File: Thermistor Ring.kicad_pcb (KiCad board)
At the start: 2 copper layers, 70 x 70 mm, 20 parts, among them IC1 MAX30210ENL+, IC2 MAX30210ENL+, IC3 MAX30210ENL+, IC4 MAX30210ENL+, IC5 MAX30210ENL+, IC6 MAX30210ENL+, J1 Conn_01x04_Socket, J3 Conn_01x03_Socket, U1 TPS7A2018PDBVR

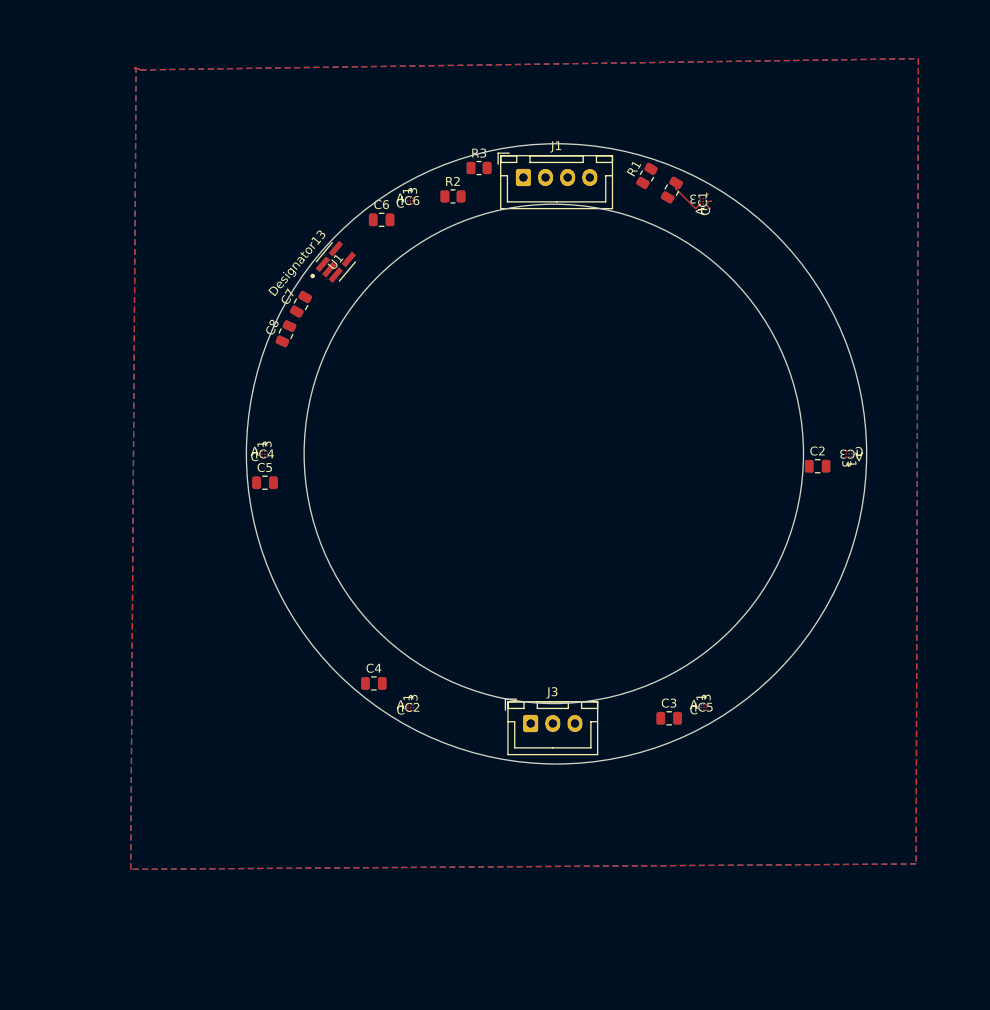
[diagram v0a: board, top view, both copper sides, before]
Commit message: saving before moving thermistors
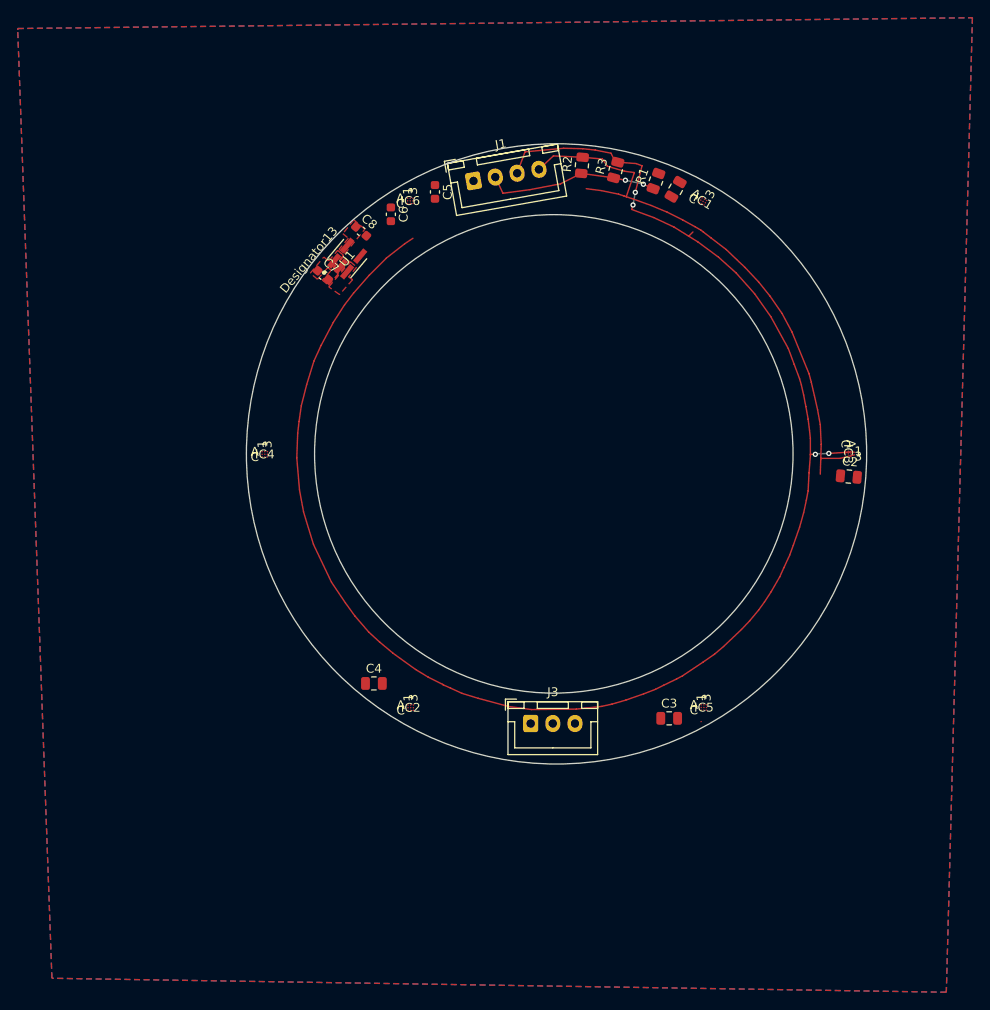
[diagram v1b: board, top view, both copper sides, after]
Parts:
- C5, C6, C7, C8: footprint Capacitor_SMD:C_0805_2012Metric -> Capacitor_SMD:C_0603_1608Metric
- moved C5 38.0 mm to (200.2, 41.6), turned to -90 degrees
- moved R3 15.4 mm to (220.6, 39.1), turned to 75 degrees
- moved R2 15.0 mm to (216.8, 38.6), turned to 85 degrees
- moved C8 14.3 mm to (191.9, 46.0), turned to -40 degrees
- moved J1 5.64 mm to (204.5, 40.3), turned to 10 degrees
- moved C7 4.13 mm to (187.6, 50.9), turned to -40 degrees
- moved C2 3.70 mm to (246.9, 73.7), turned to -5 degrees
- moved U1 1.34 mm to (190.3, 49.1)
- moved C6 1.21 mm to (195.2, 44.1), turned to -90 degrees
- moved R1 1.16 mm to (225.1, 40.3), turned to 70 degrees
- moved C1 0.43 mm to (227.4, 41.3), turned to 60 degrees
- moved IC3 0.10 mm to (246.8, 71.1), turned to -90 degrees
- turned IC1 to -30 degrees
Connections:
- net Net-(IC1-VDD) renamed /VDD
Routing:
- net /SDA: track 0.74 -> 183.6 mm, vias 0 -> 4
- net /SCL: track 0.66 -> 64.7 mm
- net /Power 3.3-5V: track 0.00 -> 19.6 mm, vias 0 -> 2
- net /VDD: track 4.57 -> 0.00 mm
- net /CVT/PDB: track 0.83 -> 0.00 mm
- added copper zone on F.Cu, net /ENABLE
- added copper zone on F.Cu, net /Power 3.3-5V
- added copper zone on F.Cu, net /VDD
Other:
- outline, holes or cut-outs redrawn

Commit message: v0.1 alpha for review
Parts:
- U1: footprint LDO_TSA7A:DBV0005A-IPC_A -> TPS7A201:DBV0005A-IPC_A
- moved R2 32.3 mm to (188.1, 53.6), turned to -35 degrees
- moved R3 32.1 mm to (190.6, 50.5), turned to -40 degrees
- moved R1 32.0 mm to (193.9, 47.3), turned to -50 degrees
- moved C6 26.2 mm to (182.8, 67.2), turned to -10 degrees
- moved C8 19.2 mm to (184.8, 63.9), turned to 160 degrees
- moved U1 12.9 mm to (185.2, 61.0), turned to -110 degrees
- moved C1 7.66 mm to (232.8, 46.7), turned to -130 degrees
- moved C7 7.40 mm to (187.2, 58.3), turned to 160 degrees
- moved J3 5.28 mm to (216.3, 102.1), turned to 180 degrees
- moved C2 2.59 mm to (244.4, 74.3)
- moved C4 2.36 mm to (195.5, 96.3), turned to 55 degrees
- moved IC5 2.27 mm to (229.1, 98.0), turned to -150 degrees
- moved IC3 2.24 mm to (244.6, 71.1), turned to 0 degrees
- moved IC1 2.11 mm to (229.1, 44.3), turned to -100 degrees
- moved C3 1.96 mm to (224.9, 100.1), turned to 115 degrees
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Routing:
- net /VDD: track 0.00 -> 244.5 mm, vias 0 -> 20
- net /CVT/PDB: track 0.00 -> 224.6 mm, vias 0 -> 13
- net /INT: track 0.00 -> 213.3 mm, vias 0 -> 8
- net GND: track 0.00 -> 195.9 mm, vias 0 -> 18
- net /SCL: track 64.7 -> 196.8 mm, vias 0 -> 13
- net /ENABLE: track 0.00 -> 61.8 mm, vias 0 -> 4
- net /Power 3.3-5V: track 19.6 -> 38.4 mm, vias 2 -> 0
- net /SDA: track 183.6 -> 202.3 mm
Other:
- outline, holes or cut-outs redrawn

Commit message: changing to smaller diameter
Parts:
- moved IC2 123.2 mm to (75.4, 87.0)
- moved IC6 123.2 mm to (75.4, 33.3)
- moved J1 123.2 mm to (82.5, 30.3)
- moved R3 123.2 mm to (68.0, 39.6)
- moved C1 123.2 mm to (110.1, 35.7)
- moved C4 123.2 mm to (72.9, 85.3)
- moved C5 123.2 mm to (78.3, 31.8)
- moved C6 123.2 mm to (60.1, 56.2)
- moved IC1 123.2 mm to (106.4, 33.3)
- moved IC5 123.2 mm to (106.4, 87.0)
- moved R1 123.2 mm to (71.2, 36.3)
- moved U1 123.2 mm to (62.5, 50.0)
- moved C2 123.2 mm to (121.7, 63.3)
- moved C3 123.2 mm to (102.2, 89.1)
- moved C7 123.2 mm to (64.6, 47.4)
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
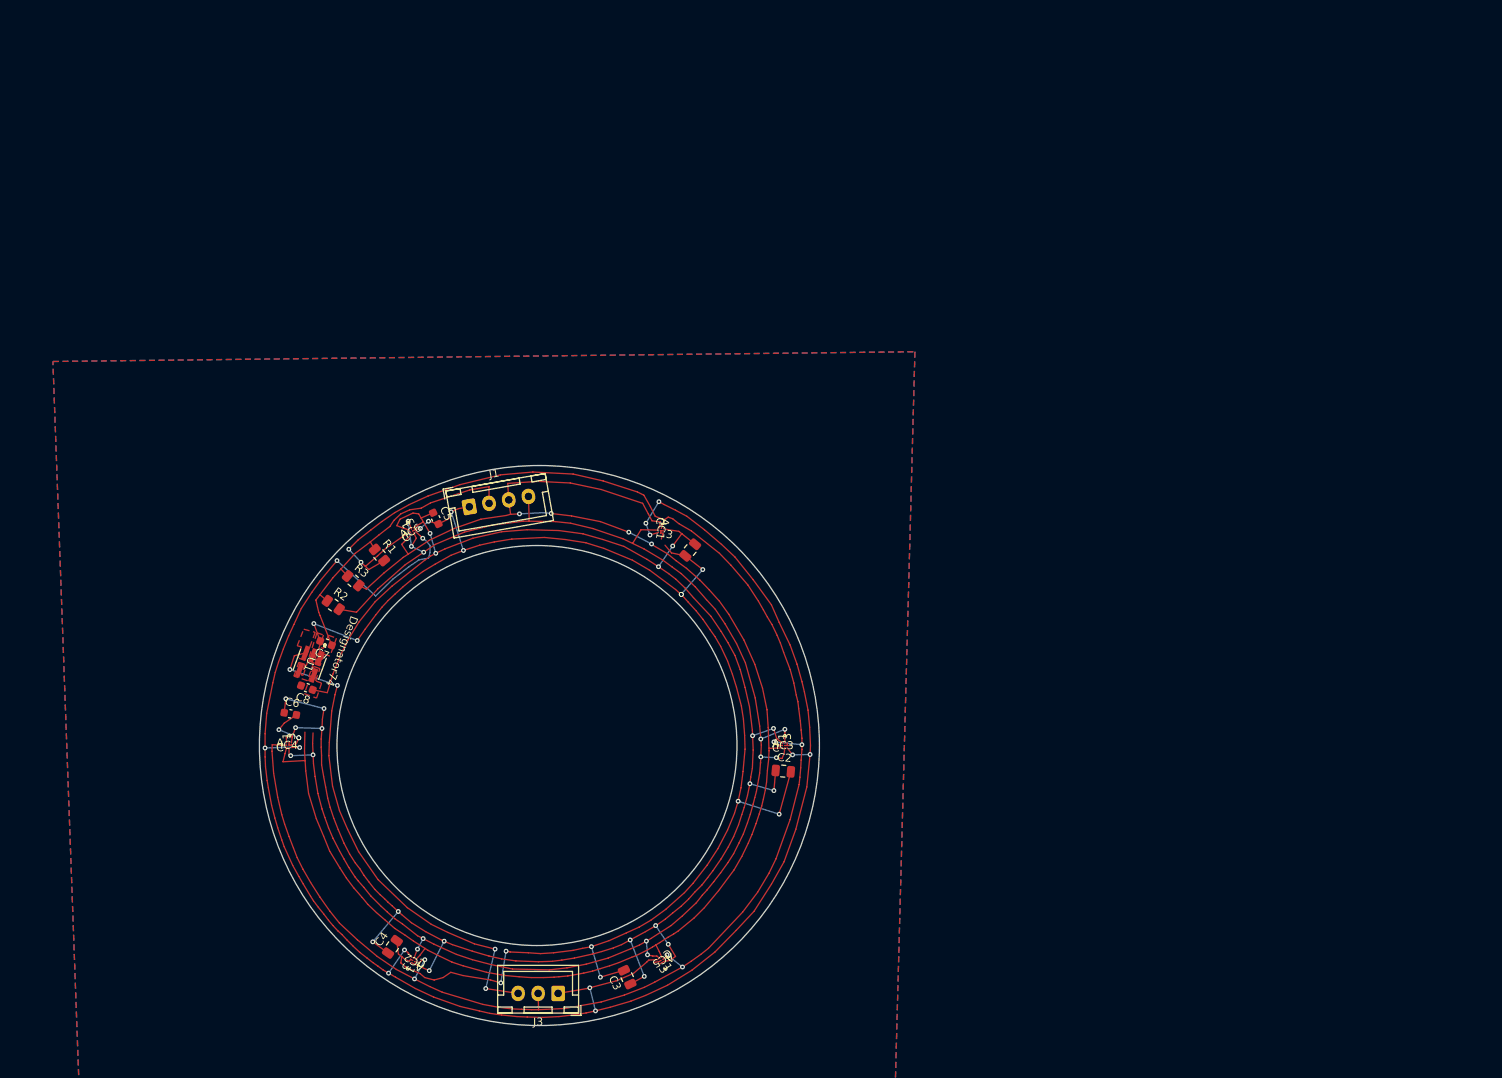
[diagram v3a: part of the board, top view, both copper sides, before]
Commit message: schematic updated for MCP9808 temperature sensor
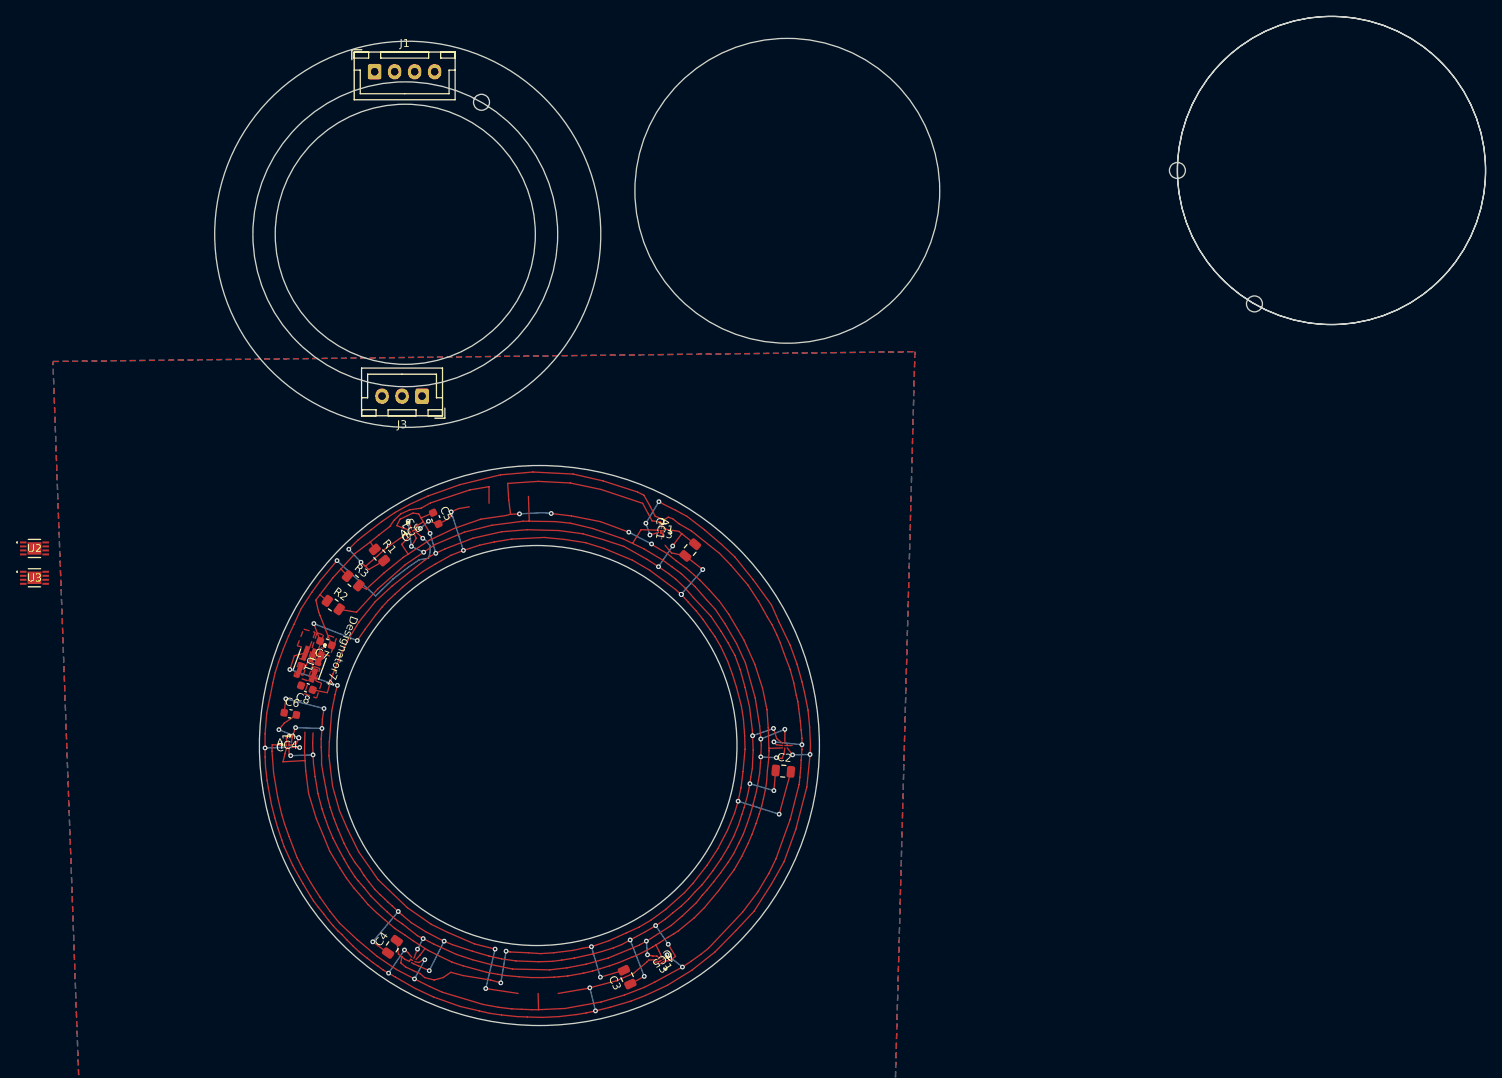
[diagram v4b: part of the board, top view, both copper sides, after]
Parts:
- removed IC2, IC3: MAX30210ENL+, MAX30210:21-100600_N90A0&plus_1_ADI
- added U2: MCP9808T-E/MC, mcp9808:DFN8_2x3MC_MCH, F.Cu at (28.1, 35.5)
- added U3: MCP9808T-E/MC, mcp9808:DFN8_2x3MC_MCH, F.Cu at (28.1, 39.2)
- moved J3 76.6 mm to (76.6, 16.5)
- moved J1 55.7 mm to (70.6, -24.1), turned to 0 degrees
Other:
- board size 70 x 70 mm -> 158.9 x 126.1 mm

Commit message: shrinking ring
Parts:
- removed IC1, IC4, IC5, IC6: MAX30210ENL+, MAX30210:21-100600_N90A0&plus_1_ADI
- removed J3: Conn_01x03_Socket, Connector_JST:JST_XH_B3B-XH-A_1x03_P2.50mm_Vertical
- added U4: MCP9808T-E/MC, mcp9808:DFN8_2x3MC_MCH, F.Cu at (84.2, 12.7)
- added U5: MCP9808T-E/MC, mcp9808:DFN8_2x3MC_MCH, F.Cu at (93.6, -3.71)
- added U6: MCP9808T-E/MC, mcp9808:DFN8_2x3MC_MCH, F.Cu at (65.0, 12.7)
- added U7: MCP9808T-E/MC, mcp9808:DFN8_2x3MC_MCH, F.Cu at (84.0, -20.2)
- moved U2 66.9 mm to (64.9, -20.3), turned to 30 degrees
- moved U3 50.9 mm to (55.4, -3.76), turned to -90 degrees
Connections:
- C1 pad 1: /VDD -> /Power 3.3-5V
- C2 pad 1: /VDD -> /Power 3.3-5V
- C3 pad 1: /VDD -> /Power 3.3-5V
- C4 pad 1: /VDD -> /Power 3.3-5V
- C5 pad 1: /VDD -> unconnected-(C5-Pad1)
- C6 pad 1: /VDD -> /Power 3.3-5V
- C8 pad 1: /VDD -> /Power 3.3-5V
- U1 pad 5: /VDD -> /Power 3.3-5V
- U2 pad 4: unconnected-(U2-GND-Pad4) -> GND
- U2 pad 6: GND -> /Power 3.3-5V
- U2 pad 7: /SCL -> unconnected-(U2-A0-Pad7)
- U2 pad 8: /VDD -> /Power 3.3-5V
- U3 pad 6: GND -> unconnected-(U3-A1-Pad6)
- U3 pad 7: /VDD -> /Power 3.3-5V
- U3 pad 8: /VDD -> /Power 3.3-5V
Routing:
- net (no net): track 0.00 -> 469.1 mm, vias 0 -> 13
- net /VDD: track 244.5 -> 0.00 mm, vias 20 -> 0
- net /CVT/PDB: track 224.6 -> 0.00 mm, vias 13 -> 0
- net /Power 3.3-5V: vias 0 -> 20
- removed copper zone on F.Cu, net /VDD
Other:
- outline, holes or cut-outs redrawn
